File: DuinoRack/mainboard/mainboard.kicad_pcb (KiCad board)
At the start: 2 copper layers, 39.4 x 107.9 mm, 21 parts, among them J1 ISP, J2 SER, U1 MCP4822, U2 ATmega328P-P, U3 TL074, Y1 16MHz

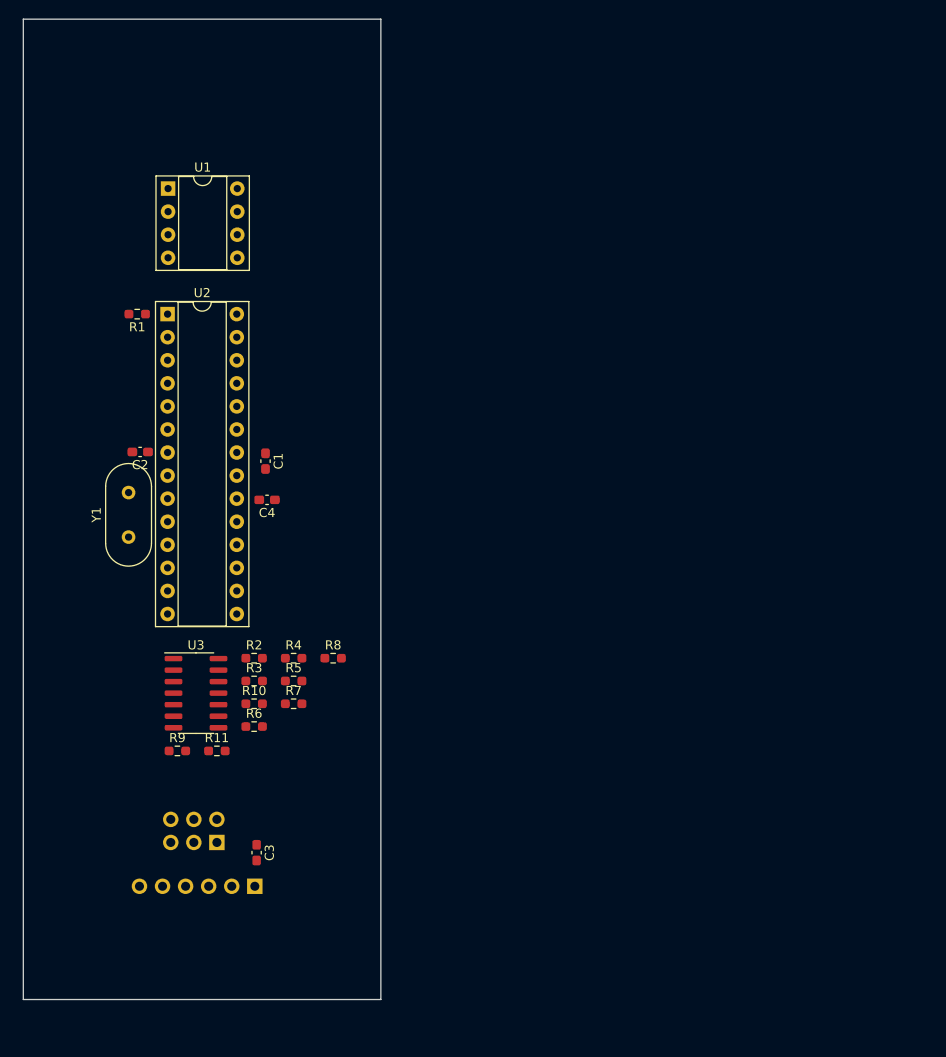
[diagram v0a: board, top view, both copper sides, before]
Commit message: Add MIDI input module and test hardware
Were removing gate input 3, since there's no way to handle the inversion.
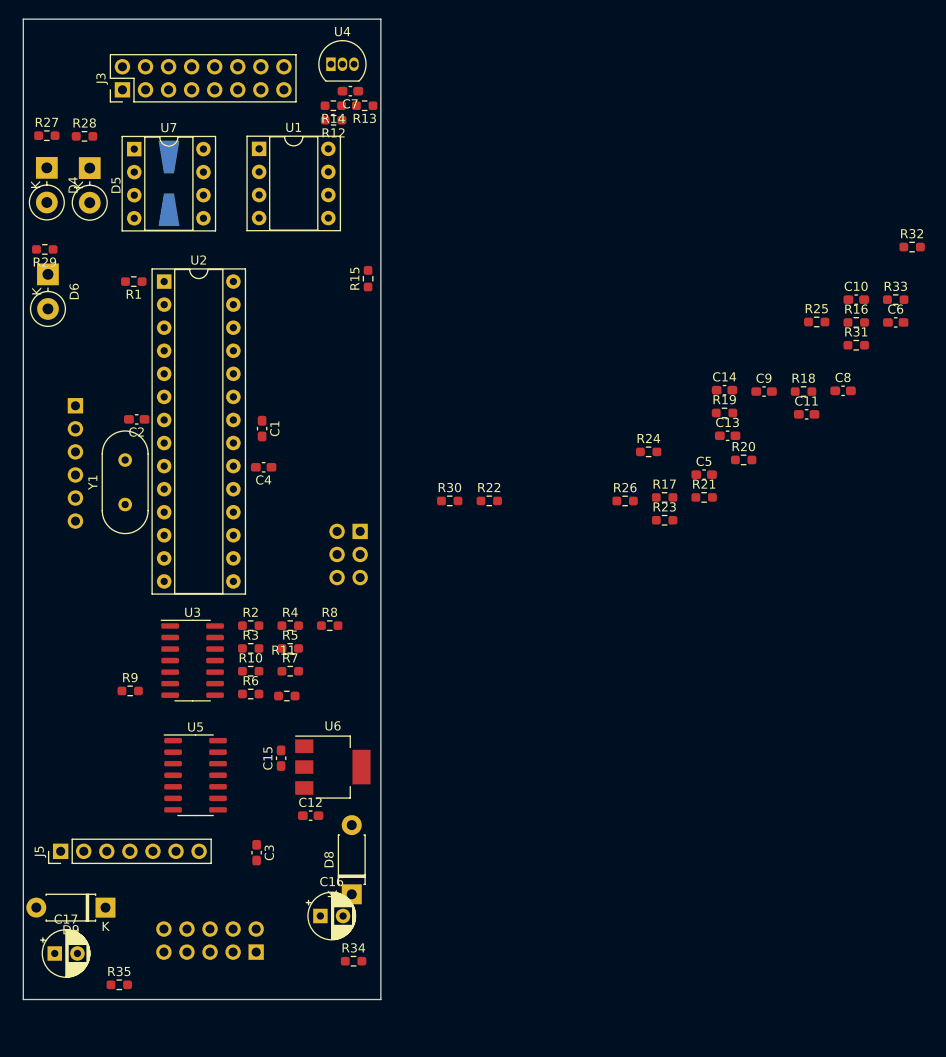
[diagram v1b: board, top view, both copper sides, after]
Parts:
- added C10: 1n, Capacitor_SMD:C_0603_1608Metric_Pad1.08x0.95mm_HandSolder, F.Cu at (184.4, 63.9)
- added C11: 1n, Capacitor_SMD:C_0603_1608Metric_Pad1.08x0.95mm_HandSolder, F.Cu at (179.0, 76.5)
- added C12: 10u, Capacitor_SMD:C_0603_1608Metric_Pad1.08x0.95mm_HandSolder, F.Cu at (124.3, 120.7)
- added C13: 18p, Capacitor_SMD:C_0603_1608Metric_Pad1.08x0.95mm_HandSolder, F.Cu at (170.3, 78.9)
- added C14: 18p, Capacitor_SMD:C_0603_1608Metric_Pad1.08x0.95mm_HandSolder, F.Cu at (169.9, 73.9)
- added C15: 10u, Capacitor_SMD:C_0603_1608Metric_Pad1.08x0.95mm_HandSolder, F.Cu at (121.1, 114.4)
- added C16: 10uF, Capacitor_THT:CP_Radial_D5.0mm_P2.50mm, F.Cu at (125.4, 131.8)
- added C17: 10uF, Capacitor_THT:CP_Radial_D5.0mm_P2.50mm, F.Cu at (96.2, 135.9)
- added C5: 100n, Capacitor_SMD:C_0603_1608Metric_Pad1.08x0.95mm_HandSolder, F.Cu at (167.7, 83.2)
- added C6: 100n, Capacitor_SMD:C_0603_1608Metric_Pad1.08x0.95mm_HandSolder, F.Cu at (188.8, 66.4)
- added C7: 100n, Capacitor_SMD:C_0603_1608Metric_Pad1.08x0.95mm_HandSolder, F.Cu at (128.7, 41.0)
- added C8: 100n, Capacitor_SMD:C_0603_1608Metric_Pad1.08x0.95mm_HandSolder, F.Cu at (183.0, 73.9)
- added C9: 1n, Capacitor_SMD:C_0603_1608Metric_Pad1.08x0.95mm_HandSolder, F.Cu at (174.3, 74.0)
- added D4: D_Zener_4.7V, Diode_THT:D_DO-15_P3.81mm_Vertical_KathodeUp, F.Cu at (95.3, 49.4)
- added D5: D_Zener_4.7V, Diode_THT:D_DO-15_P3.81mm_Vertical_KathodeUp, F.Cu at (100.0, 49.4)
- added D6: D_Zener_4.7V, Diode_THT:D_DO-15_P3.81mm_Vertical_KathodeUp, F.Cu at (95.4, 61.1)
- added D7: D, Diode_SMD:D_SMA-SMB_Universal_Handsoldering, B.Cu at (108.8, 51.1)
- added D8: 1N4007, Diode_THT:D_DO-41_SOD81_P7.62mm_Horizontal, F.Cu at (128.9, 129.4)
- added D9: 1N4007, Diode_THT:D_DO-41_SOD81_P7.62mm_Horizontal, F.Cu at (101.8, 130.8)
- added J3: Conn_02x08_Odd_Even, Connector_PinHeader_2.54mm:PinHeader_2x08_P2.54mm_Vertical, F.Cu at (103.6, 40.8)
- added J4: Conn_02x05_Odd_Even, Connector_PinHeader_2.54mm:PinHeader_2x05_P2.54mm_Vertical, B.Cu at (118.3, 135.8)
- added J5: Conn_MIDI, Connector_PinHeader_2.54mm:PinHeader_1x07_P2.54mm_Vertical, F.Cu at (96.8, 124.7)
- added R12: 1k, Resistor_SMD:R_0603_1608Metric_Pad0.98x0.95mm_HandSolder, F.Cu at (126.9, 44.1)
- added R13: 220k 0.1%, Resistor_SMD:R_0603_1608Metric_Pad0.98x0.95mm_HandSolder, F.Cu at (130.3, 42.5)
- added R14: 105k 0.1%, Resistor_SMD:R_0603_1608Metric_Pad0.98x0.95mm_HandSolder, F.Cu at (126.8, 42.5)
- added R15: 220, Resistor_SMD:R_0603_1608Metric_Pad0.98x0.95mm_HandSolder, F.Cu at (130.7, 61.6)
- added R16: 220, Resistor_SMD:R_0603_1608Metric_Pad0.98x0.95mm_HandSolder, F.Cu at (184.4, 66.4)
- added R17: 100k, Resistor_SMD:R_0603_1608Metric_Pad0.98x0.95mm_HandSolder, F.Cu at (163.3, 85.7)
- added R18: 100k, Resistor_SMD:R_0603_1608Metric_Pad0.98x0.95mm_HandSolder, F.Cu at (178.6, 74.0)
- added R19: 220, Resistor_SMD:R_0603_1608Metric_Pad0.98x0.95mm_HandSolder, F.Cu at (169.9, 76.4)
- added R20: 18k, Resistor_SMD:R_0603_1608Metric_Pad0.98x0.95mm_HandSolder, F.Cu at (172.0, 81.6)
- added R21: 4.7k, Resistor_SMD:R_0603_1608Metric_Pad0.98x0.95mm_HandSolder, F.Cu at (167.7, 85.7)
- added R22: 18k, Resistor_SMD:R_0603_1608Metric_Pad0.98x0.95mm_HandSolder, F.Cu at (144.0, 86.1)
- added R23: 1k, Resistor_SMD:R_0603_1608Metric_Pad0.98x0.95mm_HandSolder, F.Cu at (163.3, 88.2)
- added R24: 1k, Resistor_SMD:R_0603_1608Metric_Pad0.98x0.95mm_HandSolder, F.Cu at (161.6, 80.7)
- added R25: 470, Resistor_SMD:R_0603_1608Metric_Pad0.98x0.95mm_HandSolder, F.Cu at (180.1, 66.4)
- added R26: 220, Resistor_SMD:R_0603_1608Metric_Pad0.98x0.95mm_HandSolder, F.Cu at (159.0, 86.1)
- added R27: 1k, Resistor_SMD:R_0603_1608Metric_Pad0.98x0.95mm_HandSolder, F.Cu at (95.3, 45.9)
- added R28: 1k, Resistor_SMD:R_0603_1608Metric_Pad0.98x0.95mm_HandSolder, F.Cu at (99.5, 45.9)
- added R29: 1k, Resistor_SMD:R_0603_1608Metric_Pad0.98x0.95mm_HandSolder, F.Cu at (95.1, 58.4)
- added R30: 10k, Resistor_SMD:R_0603_1608Metric_Pad0.98x0.95mm_HandSolder, F.Cu at (139.7, 86.1)
- added R31: 220, Resistor_SMD:R_0603_1608Metric_Pad0.98x0.95mm_HandSolder, F.Cu at (184.4, 68.9)
- added R32: 220, Resistor_SMD:R_0603_1608Metric_Pad0.98x0.95mm_HandSolder, F.Cu at (190.6, 58.1)
- added R33: 220, Resistor_SMD:R_0603_1608Metric_Pad0.98x0.95mm_HandSolder, F.Cu at (188.8, 63.9)
- added R34: 10, Resistor_SMD:R_0603_1608Metric_Pad0.98x0.95mm_HandSolder, F.Cu at (129.1, 136.8)
- added R35: 10, Resistor_SMD:R_0603_1608Metric_Pad0.98x0.95mm_HandSolder, F.Cu at (103.3, 139.3)
- added U4: TL431LP, Package_TO_SOT_THT:TO-92_Inline, F.Cu at (126.6, 38.0)
- added U5: MCP6004, Package_SO:SO-14_3.9x8.65mm_P1.27mm, F.Cu at (111.7, 116.3)
- added U6: LM1117-5.0, Package_TO_SOT_SMD:SOT-223-3_TabPin2, F.Cu at (126.8, 115.4)
- added U7: 6N138, Package_DIP:DIP-8_W7.62mm_Socket, F.Cu at (104.9, 47.3)
- moved J2 56.5 mm to (98.5, 75.6), turned to 180 degrees
- moved J1 37.7 mm to (129.8, 89.4), turned to 180 degrees
- moved U1 10.9 mm to (118.7, 47.3)
- moved R11 9.79 mm to (121.7, 107.5)
- moved R9 8.41 mm to (104.5, 107.0)
- moved C4 3.60 mm to (119.2, 82.4)
- moved R10 3.60 mm to (117.8, 104.8)
- moved R2 3.60 mm to (117.8, 99.8)
- moved R4 3.60 mm to (122.1, 99.8)
- moved R6 3.60 mm to (117.8, 107.3)
- moved R7 3.60 mm to (122.1, 104.8)
- moved R8 3.60 mm to (126.5, 99.8)
- moved R1 3.60 mm to (104.9, 61.9)
- moved U2 3.60 mm to (108.2, 61.9)
- moved C1 3.60 mm to (119.0, 78.1)
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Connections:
- net /RX renamed /MIDI_THRU_4
- U1 pad 6: Net-(U1-Pad6) -> unconnected-(U1-Pad6)
- U1 pad 8: Net-(U1-Pad8) -> Net-(R15-Pad1)
- U2 pad 11: unconnected-(U2-Pad11) -> /ENC2A
- U2 pad 12: unconnected-(U2-Pad12) -> /ENC2B
- U2 pad 13: unconnected-(U2-Pad13) -> /ENC2
- U2 pad 14: unconnected-(U2-Pad14) -> /IN1_INT
- U2 pad 15: unconnected-(U2-Pad15) -> /IN2_INT
- U2 pad 23: unconnected-(U2-Pad23) -> /CV1
- U2 pad 24: unconnected-(U2-Pad24) -> /CV2
- U2 pad 25: unconnected-(U2-Pad25) -> /OUT1_INT
- U2 pad 26: unconnected-(U2-Pad26) -> /OUT2_INT
- U2 pad 4: unconnected-(U2-Pad4) -> /ENC1A
- U2 pad 5: unconnected-(U2-Pad5) -> /ENC1B
- U2 pad 6: unconnected-(U2-Pad6) -> /ENC1
- U3 pad 10: unconnected-(U3-Pad10) -> /OUT2_INT
- U3 pad 11: unconnected-(U3-Pad11) -> -12V
- U3 pad 12: unconnected-(U3-Pad12) -> /OUT1_INT
- U3 pad 13: unconnected-(U3-Pad13) -> Net-(R23-Pad1)
- U3 pad 14: unconnected-(U3-Pad14) -> Net-(R23-Pad1)
- U3 pad 3: Net-(U1-Pad8) -> /OUTA_INT
- U3 pad 4: unconnected-(U3-Pad4) -> +12V
- U3 pad 5: Net-(U1-Pad6) -> /OUTB_INT
- U3 pad 8: unconnected-(U3-Pad8) -> Net-(R24-Pad1)
- U3 pad 9: unconnected-(U3-Pad9) -> Net-(R24-Pad1)

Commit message: Add programming jumper, fix up MIDI in and THRU
We need to disconnect midi in during programming, since it will pull up
RX. Hence the new jumper.
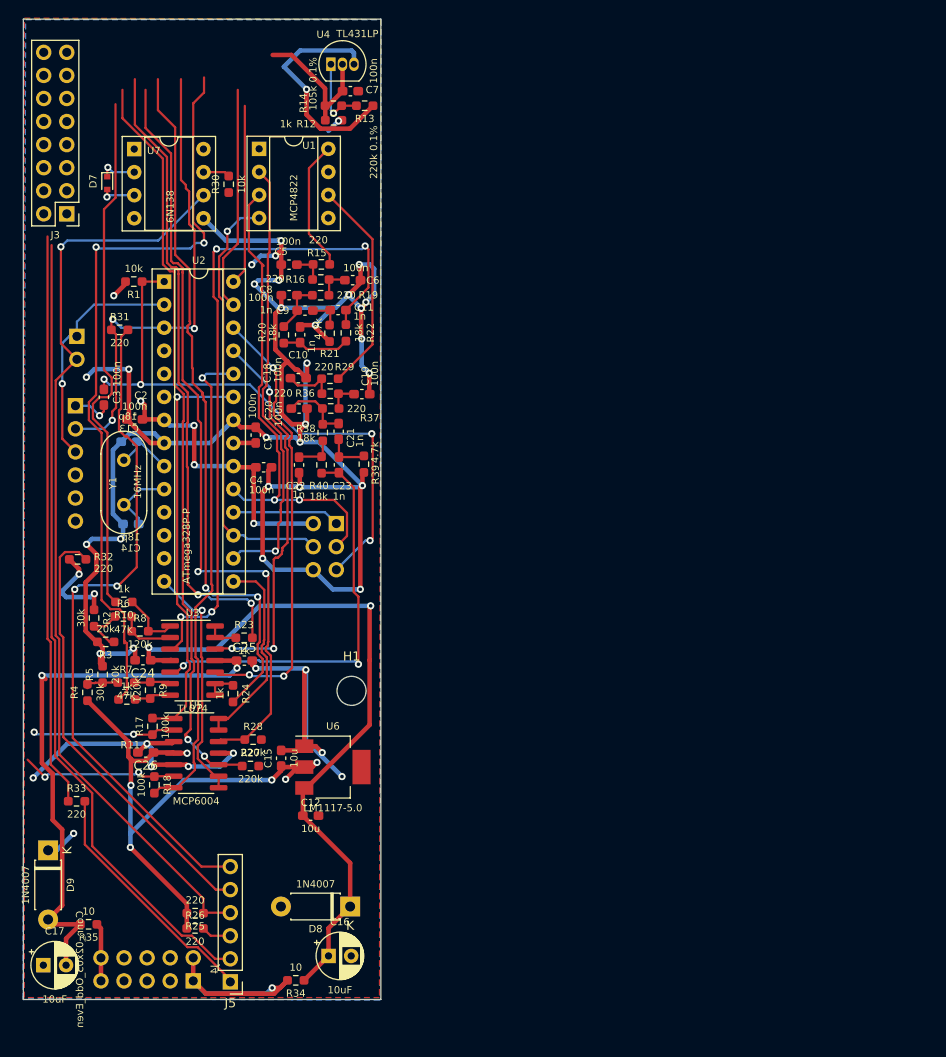
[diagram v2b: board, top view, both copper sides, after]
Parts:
- removed D4, D5, D6: D_Zener_4.7V, Diode_THT:D_DO-15_P3.81mm_Vertical_KathodeUp
- added C18: 100n, Capacitor_SMD:C_0603_1608Metric_Pad1.08x0.95mm_HandSolder, F.Cu at (123.0, 72.5)
- added C19: 100n, Capacitor_SMD:C_0603_1608Metric_Pad1.08x0.95mm_HandSolder, F.Cu at (130.0, 74.3)
- added C20: 100n, Capacitor_SMD:C_0603_1608Metric_Pad1.08x0.95mm_HandSolder, F.Cu at (123.1, 75.9)
- added C21: 1n, Capacitor_SMD:C_0603_1608Metric_Pad1.08x0.95mm_HandSolder, F.Cu at (127.4, 78.4)
- added C22: 1n, Capacitor_SMD:C_0603_1608Metric_Pad1.08x0.95mm_HandSolder, F.Cu at (123.1, 82.1)
- added C23: 1n, Capacitor_SMD:C_0603_1608Metric_Pad1.08x0.95mm_HandSolder, F.Cu at (127.5, 82.1)
- added C24: 100n, Capacitor_SMD:C_0603_1608Metric_Pad1.08x0.95mm_HandSolder, F.Cu at (105.9, 103.6)
- added C25: 100n, Capacitor_SMD:C_0603_1608Metric_Pad1.08x0.95mm_HandSolder, F.Cu at (117.0, 103.7)
- added C26: 100n, Capacitor_SMD:C_0603_1608Metric_Pad1.08x0.95mm_HandSolder, F.Cu at (106.2, 113.8)
- added H1: MountingHole, MountingHole:MountingHole_3.2mm_M3_DIN965, F.Cu at (128.8, 107.0)
- added JP1: !PROGRAM, Connector_PinHeader_2.54mm:PinHeader_1x02_P2.54mm_Vertical, B.Cu at (98.6, 67.9)
- added R36: 220, Resistor_SMD:R_0603_1608Metric_Pad0.98x0.95mm_HandSolder, F.Cu at (126.5, 74.3)
- added R37: 220, Resistor_SMD:R_0603_1608Metric_Pad0.98x0.95mm_HandSolder, F.Cu at (126.6, 75.9)
- added R38: 18k, Resistor_SMD:R_0603_1608Metric_Pad0.98x0.95mm_HandSolder, F.Cu at (125.7, 78.5)
- added R39: 4.7k, Resistor_SMD:R_0603_1608Metric_Pad0.98x0.95mm_HandSolder, F.Cu at (130.2, 82.0)
- added R40: 18k, Resistor_SMD:R_0603_1608Metric_Pad0.98x0.95mm_HandSolder, F.Cu at (125.5, 82.1)
- C13, C14: moved to B.Cu
- C2, C4: value C -> 100n
- D7: footprint Diode_SMD:D_SMA-SMB_Universal_Handsoldering -> Diode_SMD:D_SOD-523; moved to F.Cu
- J5: footprint Connector_PinHeader_2.54mm:PinHeader_1x07_P2.54mm_Vertical -> Connector_PinHeader_2.54mm:PinHeader_1x06_P2.54mm_Vertical
- R25: value 470 -> 220
- R27, R28: value 1k -> 220k
- R29: value 1k -> 220
- U6: footprint Package_TO_SOT_SMD:SOT-223-3_TabPin2 -> Package_TO_SOT_SMD:SOT-223
- moved R33 105.8 mm to (98.6, 119.1)
- moved R32 98.1 mm to (98.7, 92.5)
- moved R25 94.5 mm to (111.6, 131.5), turned to 180 degrees
- moved R18 83.6 mm to (107.1, 117.3), turned to -90 degrees
- moved R31 81.1 mm to (103.3, 67.2)
- moved R27 72.9 mm to (117.7, 115.3)
- moved R28 69.0 mm to (118.0, 112.3)
- moved C14 67.0 mm to (104.5, 88.6), turned to 180 degrees
- moved R26 66.8 mm to (111.6, 133.1)
- moved C13 65.9 mm to (104.3, 79.5), turned to 180 degrees
- moved C8 61.9 mm to (122.0, 63.4)
- moved R17 61.8 mm to (106.9, 110.9), turned to 90 degrees
- moved C10 61.4 mm to (123.2, 67.8), turned to 90 degrees
- moved C6 60.0 mm to (129.0, 61.8), turned to 180 degrees
- moved R16 59.1 mm to (125.5, 61.7)
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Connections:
- J2 pad 2: /TX -> /OUT3
- J2 pad 3: /MIDI_THRU_4 -> /RX
- J3 pad 15: unconnected-(J3-Pad15) -> GND
- J3 pad 5: /IN3 -> unconnected-(J3-Pad5)
- J5 pad 1: GND -> /MIDI_IN_4
- J5 pad 2: /MIDI_IN_4 -> /MIDI_IN_5
- J5 pad 3: /MIDI_IN_5 -> /MIDI_THRU_4
- J5 pad 4: /MIDI_THRU_4 -> /MIDI_THRU_5
- J5 pad 5: /MIDI_THRU_5 -> /MIDI_OUT_4
- J5 pad 6: /MIDI_OUT_4 -> /MIDI_OUT_5
- R25 pad 1: /MIDI_THRU_4 -> /MIDI_THRU_5
- R26 pad 2: /MIDI_THRU_5 -> /MIDI_THRU_4
- R27 pad 2: Net-(D4-Pad1) -> GND
- R28 pad 2: Net-(D5-Pad1) -> GND
- R29 pad 1: /IN3 -> Net-(R29-Pad1)
- R29 pad 2: /MIDI_THRU_4 -> Net-(C18-Pad2)
- R31 pad 1: /TX -> /OUT3
- R31 pad 2: /MIDI_OUT_4 -> /MIDI_OUT_5
- R32 pad 2: /MIDI_OUT_5 -> /MIDI_OUT_4
- U1 pad 6: unconnected-(U1-Pad6) -> Net-(R29-Pad1)
- U2 pad 2: /MIDI_THRU_4 -> /RX
- U2 pad 3: /TX -> /OUT3
- U5 pad 10: Net-(D4-Pad1) -> /IN1
- U5 pad 12: Net-(D5-Pad1) -> /IN2
- U7 pad 6: /MIDI_THRU_4 -> /MIDI_THRU_5
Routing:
- net GND: track 0.00 -> 322.8 mm, vias 0 -> 39
- net +5V: track 0.00 -> 108.6 mm, vias 0 -> 13
- net /MIDI_THRU_5: track 0.00 -> 102.8 mm, vias 0 -> 1
- net /MIDI_IN_5: track 0.00 -> 92.3 mm, vias 0 -> 1
- net /IN2: track 0.00 -> 86.5 mm, vias 0 -> 2
- net /OUTB: track 0.00 -> 84.5 mm, vias 0 -> 2
- net /IN1: track 0.00 -> 83.2 mm, vias 0 -> 2
- net +12V: track 0.00 -> 79.7 mm, vias 0 -> 2
- net /OUT2: track 0.00 -> 77.9 mm, vias 0 -> 2
- net /MIDI_OUT_5: track 0.00 -> 75.1 mm, vias 0 -> 2
- net /OUTA_INT: track 0.00 -> 74.9 mm, vias 0 -> 4
- net /OUT1: track 0.00 -> 70.1 mm, vias 0 -> 2
- net Net-(D7-Pad1): track 0.00 -> 67.3 mm, vias 0 -> 1
- net -12V: track 0.00 -> 65.5 mm, vias 0 -> 3
- net /RESET: track 0.00 -> 63.9 mm, vias 0 -> 4
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- added copper zone on B.Cu, net +5V
- added copper zone on F.Cu, net GND
